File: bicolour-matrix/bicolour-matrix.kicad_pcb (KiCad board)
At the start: 2 copper layers, 50 parts, among them J1 Conn_01x04_Pin, U1 HT16K33A-28SOP, U2 HT16K33A-28SOP, U3 HT16K33A-28SOP, U4 HT16K33A-28SOP

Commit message: feat: final revs
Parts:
- added C6: 10uF, PCM_JLCPCB:C_0805, F.Cu at (90.0, 90.0)
- added J2: Conn_01x04_Pin, Connector_PinHeader_2.54mm:PinHeader_1x04_P2.54mm_Vertical, F.Cu at (87.0, 83.8)
- moved R12 1.32 mm to (163.7, 81.2)
- moved R6 1.32 mm to (163.7, 82.8)
- moved R7 1.32 mm to (97.7, 82.8)
- moved R8 1.32 mm to (97.7, 81.2)
- moved R1 1.32 mm to (130.7, 82.8)
- moved R16 1.32 mm to (196.7, 82.8)
- moved R17 1.32 mm to (196.7, 81.2)
- moved R2 1.32 mm to (130.7, 81.2)
- moved D2 0.26 mm to (128.2, 94.4)
- moved R4 0.26 mm to (128.2, 91.2)
- moved C3 0.26 mm to (136.8, 87.8)
- moved C4 0.26 mm to (169.8, 87.8)
- moved C5 0.26 mm to (202.8, 87.8)
- moved D1 0.26 mm to (95.2, 94.4)
- moved D3 0.26 mm to (161.2, 94.4)
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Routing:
- net VDD: track 57.6 -> 301.4 mm, vias 8 -> 12
- net /Matrix 1/SDA: track 32.1 -> 260.8 mm
- net /Matrix 1/SCL: track 37.7 -> 251.4 mm, vias 0 -> 4
- net GND: track 21.1 -> 16.7 mm, vias 4 -> 0
- added copper zone on B.Cu, net GND
- added copper zone on F.Cu, net GND
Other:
- board outline added: 136.2 x 33.5 mm

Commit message: feat: gerbers + design feedback
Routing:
- net /Matrix 1/SDA: track 260.8 -> 255.4 mm
- net VDD: track 301.4 -> 302.3 mm
- net /Matrix 1/SCL: track 251.4 -> 251.6 mm, vias 4 -> 5
- net GND: vias 0 -> 49
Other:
- outline, holes or cut-outs redrawn
- board text added: "GND"
- board text added: "SCL"
- board text added: "SDA"
- board text added: "VDD"

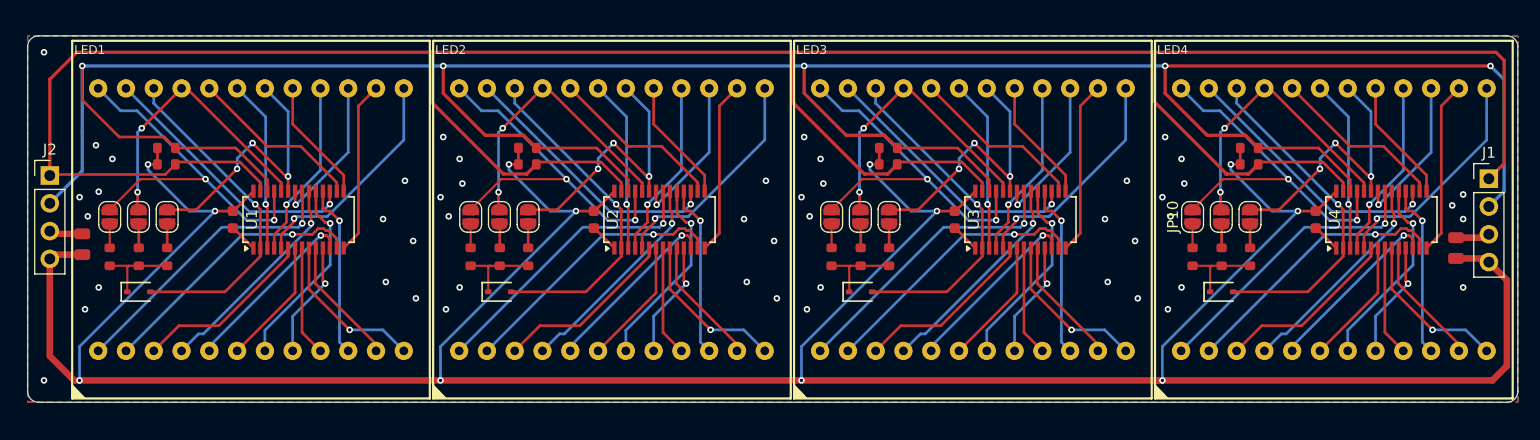
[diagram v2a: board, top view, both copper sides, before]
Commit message: feat: adapter board
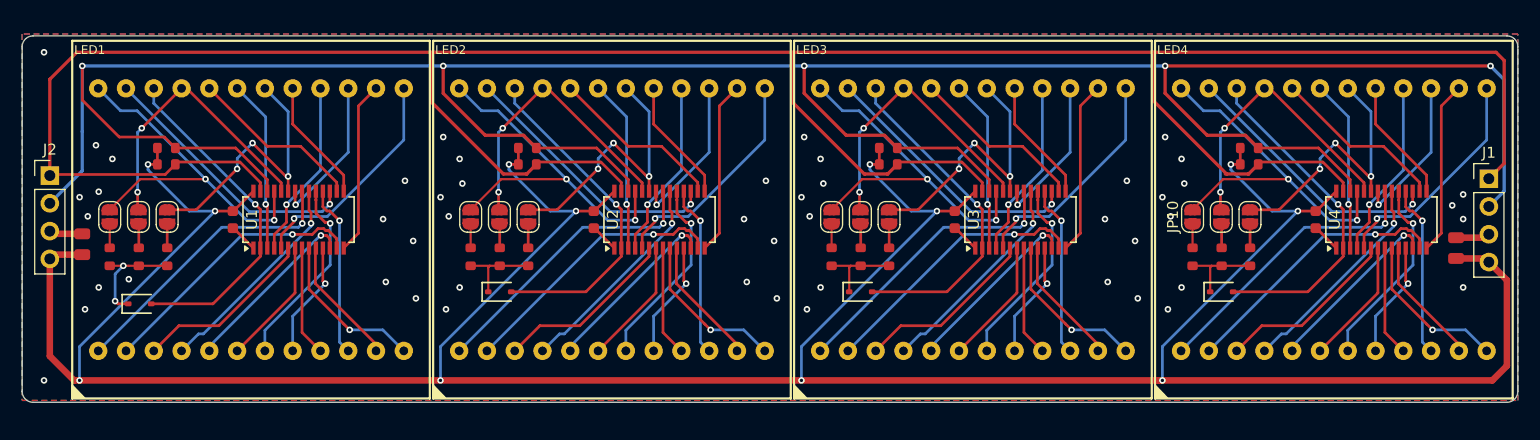
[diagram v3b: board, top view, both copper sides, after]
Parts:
- moved D1 1.10 mm to (95.2, 95.5)
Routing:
- net Net-(D1-Pad1): track 7.76 -> 10.2 mm, vias 0 -> 2
- net GND: vias 49 -> 50
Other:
- board size 136.2 x 33.5 mm -> 136.8 x 33.5 mm
